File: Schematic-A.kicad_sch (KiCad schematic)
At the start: 42 parts, among them Q1 2N7002, U11 SAM-M10Q-00B, U3 ICM-45686, U6 ICP-20100, U8 MMC5983MA

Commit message: GPS connections made
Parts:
- added C32, C37: 100nF, PCM_JLCPCB:C_0402, symbol PCM_JLCPCB-Capacitors:0402,100nF
- added R5: 10kΩ, PCM_JLCPCB:R_0402, symbol PCM_JLCPCB-Resistors:0402,10kΩ
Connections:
- net +3V3_SENSORS: now also U11.17 (VCC), U11.2 (V_IO), U11.3 (V_BCKP), C32.1, C37.1, R5.2
- net GND: now also U11.1 (GND), U11.10 (GND), U11.11 (GND), U11.15 (GND), U11.16 (GND), U11.20 (GND), U11.4 (GND), U11.5 (GND), U11.6 (GND), C32.2, C37.2
- net GPS_TX: now reaches U11.13 (TXD)
- net GPS_RX: now reaches U11.14 (RXD)
- net at U11.18 (RESET_N): now also R5.1
- net GPS_LOCK: now reaches U11.7 (TIMEPULSE)
- no-connect marks 7 -> 11
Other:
- note added: "TIMEPULSE can only source/sink 2mA."
- note added: "The TIMEPULSE pin (Pin 7) outputs a 1 pulse per second (1PPS) signal once a fix is acquired. Before fix it is typically silent (no pulse)."

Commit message: Cleaned up circuit
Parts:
- R15: value 0402WGF1000TCE -> 100
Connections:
- net GND: now also BUZZER2.3, BUZZER2.4
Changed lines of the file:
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@@
 	(text "The TIMEPULSE pin (Pin 7) outputs a 1 pulse per second (1PPS) signal once a fix is acquired.\n Before fix it is typically silent (no pulse)."
 		(exclude_from_sim no)
-		(at 239.268 104.14 0)
+		(at 234.696 103.124 0)
 		(effects
 			(font
@@
 	(text "TIMEPULSE can only source/sink 2mA."
 		(exclude_from_sim no)
-		(at 237.236 109.22 0)
+		(at 232.918 108.458 0)
 		(effects
 			(font
@@
 	)
 	(symbol
+		(lib_id "power:GND")
+		(at 58.42 139.7 0)
+		(unit 1)
+		(exclude_from_sim no)
+		(in_bom yes)
+		(on_board yes)
+		(dnp no)
+		(fields_autoplaced yes)
+		(property "Reference" "#PWR094"
+			(at 58.42 146.05 0)
+			(effects
+				(font
+					(size 1.27 1.27)
+				)
+				(hide yes)
+			)
+		)
+		(property "Value" "GND"
+			(at 58.42 144.78 0)
+			(effects
+				(font
+					(size 1.27 1.27)
+				)
+			)
+		)
+		(property "Footprint" ""
+			(at 58.42 139.7 0)
+			(effects
+				(font
+					(size 1.27 1.27)
+				)
+				(hide yes)
+			)
+		)
+		(property "Datasheet" ""
+			(at 58.42 139.7 0)
+			(effects
+				(font
+					(size 1.27 1.27)
+				)
+				(hide yes)
+			)
+		)
+		(property "Description" "Power symbol creates a global label with name \"GND\" , ground"
+			(at 58.42 139.7 0)
+			(effects
+				(font
+					(size 1.27 1.27)
+				)
+				(hide yes)
+			)
+		)
+		(pin "1"
+		)
+		(instances
+			(project "ChariotFC"
+				(path "/f9038082-7277-4432-8261-819b532197cb/27820f9d-3ddc-4a6b-9676-8f0d962bdc04"
+					(reference "#PWR094")
+					(unit 1)
+				)
+			)
+		)
+	)
+	(symbol
 		(lib_id "Connector:TestPoint")
 		(at 241.3 27.94 90)
@@
 	(symbol
 		(lib_id "power:GND")
+		(at 58.42 132.08 180)
+		(unit 1)
+		(exclude_from_sim no)
+		(in_bom yes)
+		(on_board yes)
+		(dnp no)
+		(fields_autoplaced yes)
+		(property "Reference" "#PWR095"
+			(at 58.42 125.73 0)
+			(effects
+				(font
+					(size 1.27 1.27)
+				)
+				(hide yes)
+			)
+		)
+		(property "Value" "GND"
+			(at 58.42 127 0)
+			(effects
+				(font
+					(size 1.27 1.27)
+				)
+			)
+		)
+		(property "Footprint" ""
+			(at 58.42 132.08 0)
+			(effects
+				(font
+					(size 1.27 1.27)
+				)
+				(hide yes)
+			)
+		)
+		(property "Datasheet" ""
+			(at 58.42 132.08 0)
+			(effects
+				(font
+					(size 1.27 1.27)
+				)
+				(hide yes)
+			)
+		)
+		(property "Description" "Power symbol creates a global label with name \"GND\" , ground"
+			(at 58.42 132.08 0)
+			(effects
+				(font
+					(size 1.27 1.27)
+				)
+				(hide yes)
+			)
+		)
+		(pin "1"
+		)
+		(instances
+			(project "ChariotFC"
+				(path "/f9038082-7277-4432-8261-819b532197cb/27820f9d-3ddc-4a6b-9676-8f0d962bdc04"
+					(reference "#PWR095")
+					(unit 1)
+				)
+			)
+		)
+	)
+	(symbol
+		(lib_id "power:GND")
 		(at 48.26 152.4 0)
 		(unit 1)
@@
 		(fields_autoplaced yes)
 		(property "Reference" "R15"
-			(at 35.56 140.97 0)
+			(at 35.56 143.51 0)
 			(effects
 				(font
@@
 			)
 		)
-		(property "Value" "0402WGF1000TCE"
-			(at 35.56 143.51 0)
+		(property "Value" "100"
+			(at 35.56 144.78 0)
 			(effects
 				(font

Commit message: Added PWR flags, Changed MCU pins electrical characteristics to bidirectional, rectified some ERC errors
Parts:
- renumbered BUZZER2 to BUZZER1, C19 to C22, C16 to C23, C21 to C24, C20 to C25, C17 to C26, C14 to C27, C15 to C28, C18 to C29, C32 to C30, C37 to C31, D1 to D3, LED2 to LED4, R15 to R12, R20 to R13, R4 to R14, R18 to R15, R17 to R16, R16 to R17, R19 to R18, R5 to R19, TP2 to TP1, TP5 to TP10, TP18 to TP11, TP19 to TP12, TP4 to TP13, TP16 to TP14, TP17 to TP15, TP7 to TP16, TP20 to TP17, TP21 to TP18, TP1 to TP2, TP8 to TP3, TP9 to TP4, TP3 to TP5, TP10 to TP6, TP6 to TP7, TP11 to TP8, TP15 to TP9, U11 to U10, U8 to U7, U3 to U8, U6 to U9
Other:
- note added: "GNSS"
- moved on the sheet: C30, C31, LED3, LED4, R19, U10

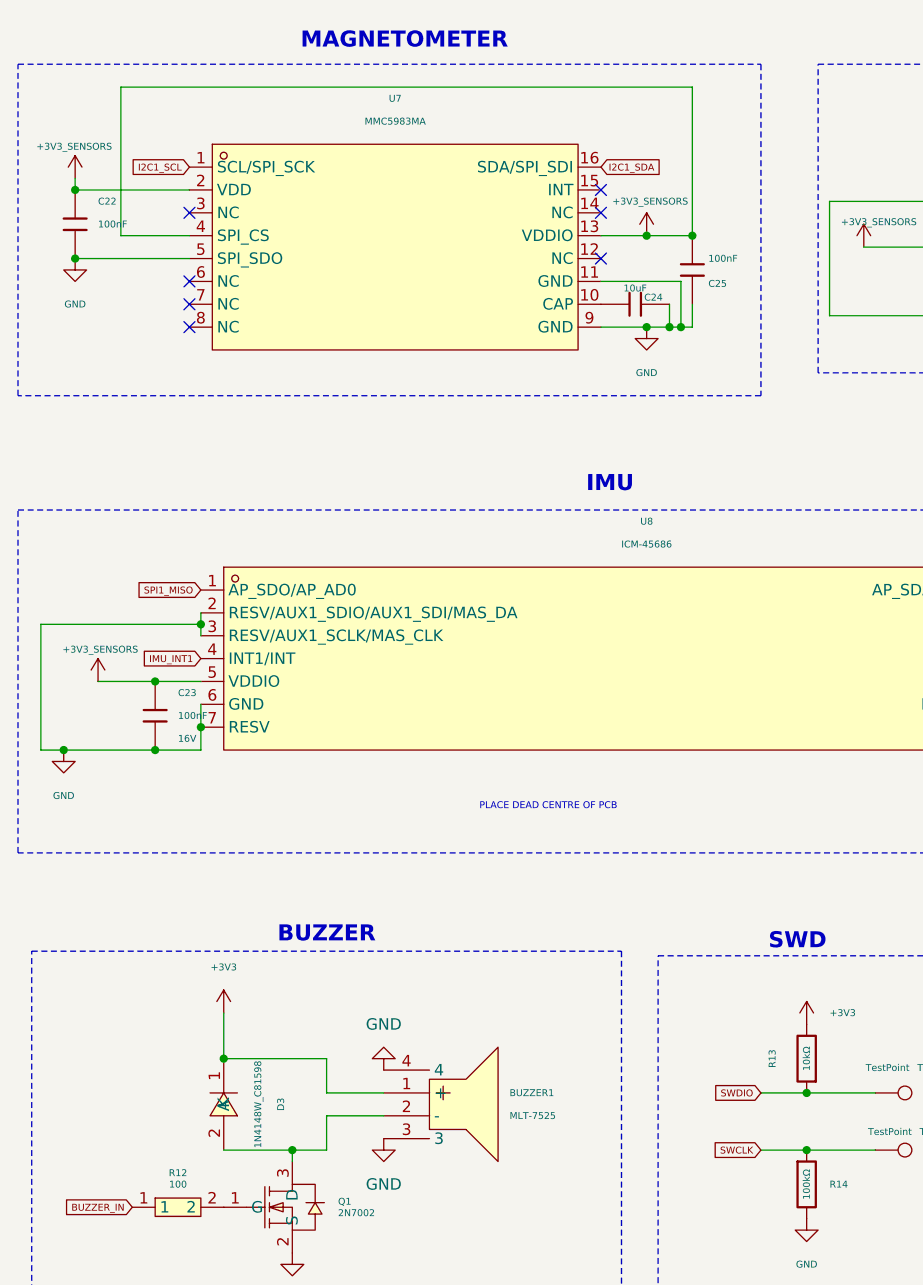
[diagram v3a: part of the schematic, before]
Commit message: Put the orrect load capacitances fo the External Osc
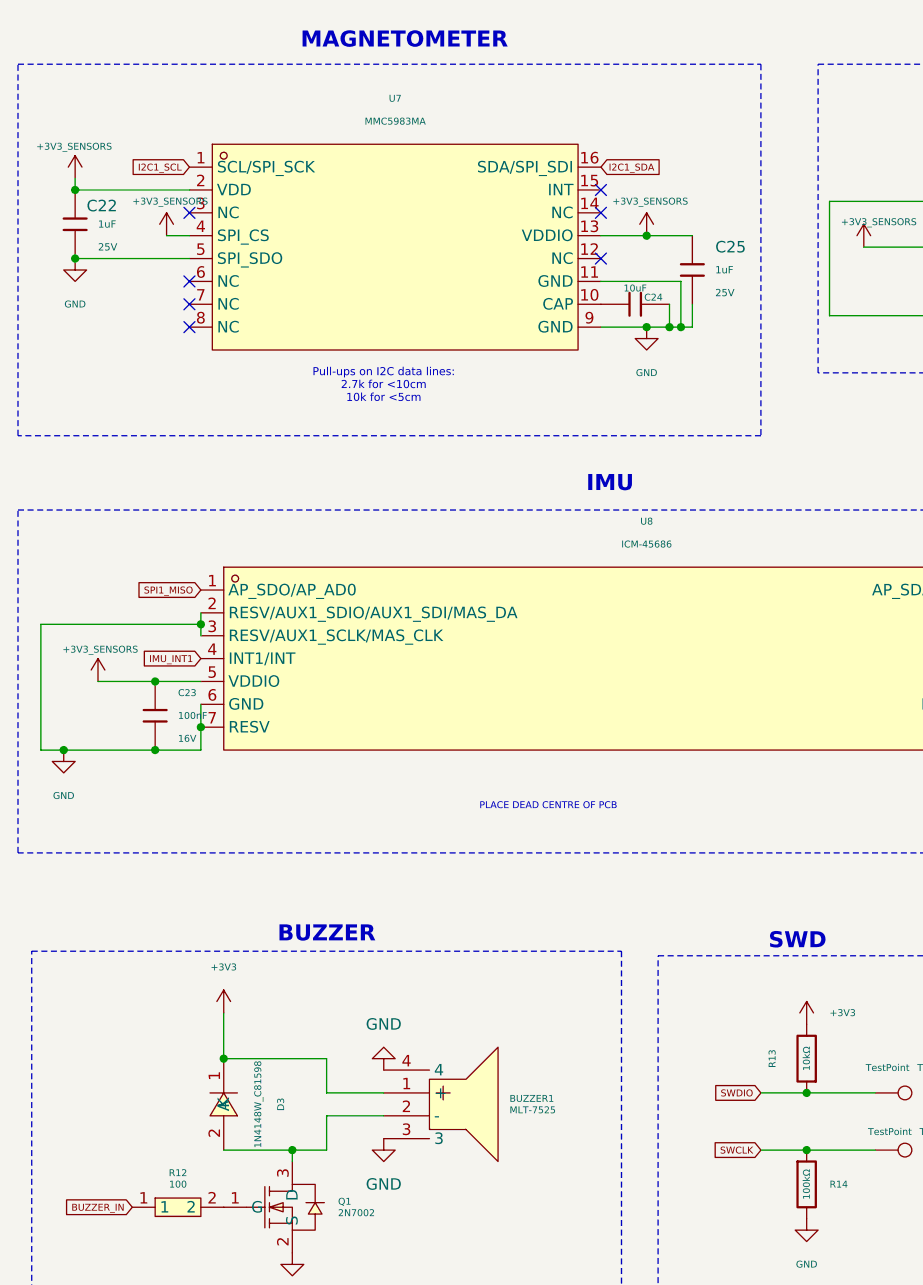
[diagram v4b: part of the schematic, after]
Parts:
- removed C22, C25: 100nF, PCM_JLCPCB:C_0402, symbol PCM_JLCPCB-Capacitors:0402,100nF
- added C22, C25: 1uF, PCM_JLCPCB:C_0402, symbol PCM_JLCPCB-Capacitors:0402,1uF
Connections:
- net +3V3_SENSORS: now also C22.1, C25.1
- net GND: now also C22.2, C25.2
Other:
- note added: "Pull-ups on I2C data lines: 2.7k for <10cm 10k for <5cm"
